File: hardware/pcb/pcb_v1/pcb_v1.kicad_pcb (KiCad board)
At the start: 2 copper layers, 181.4 x 151.5 mm, 21 parts, among them J1 Conn_01x10, J2 Conn_01x10, J3 Conn_01x10, J4 Conn_01x10, U1 Pico

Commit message: pcbv1 updated (MC34166 added)
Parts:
- added D17: 1N5822, Diode_THT:D_DO-201AD_P15.24mm_Horizontal, F.Cu at (184.4, 83.5)
- added U2: MC34166, Package_TO_SOT_SMD:TO-263-5_TabPin3, F.Cu at (175.4, 58.9)

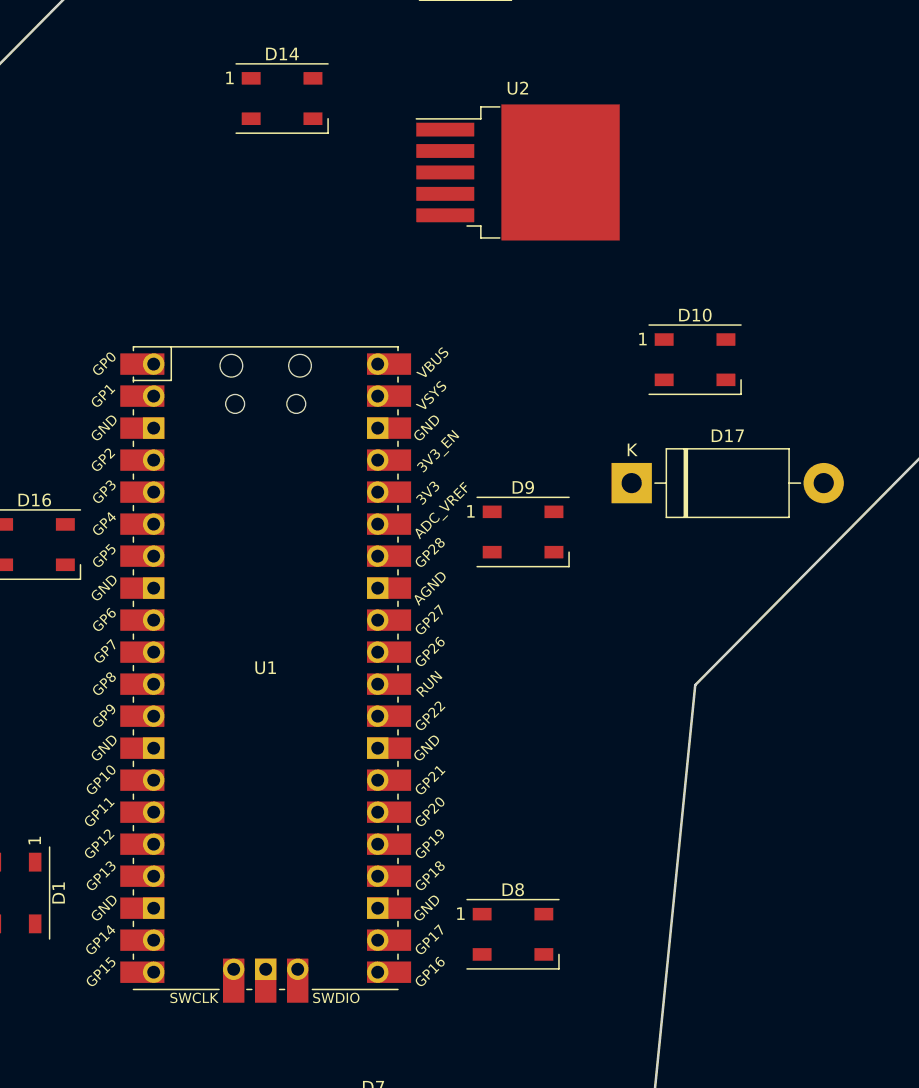
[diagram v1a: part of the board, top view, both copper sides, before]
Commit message: TL2575-05 added
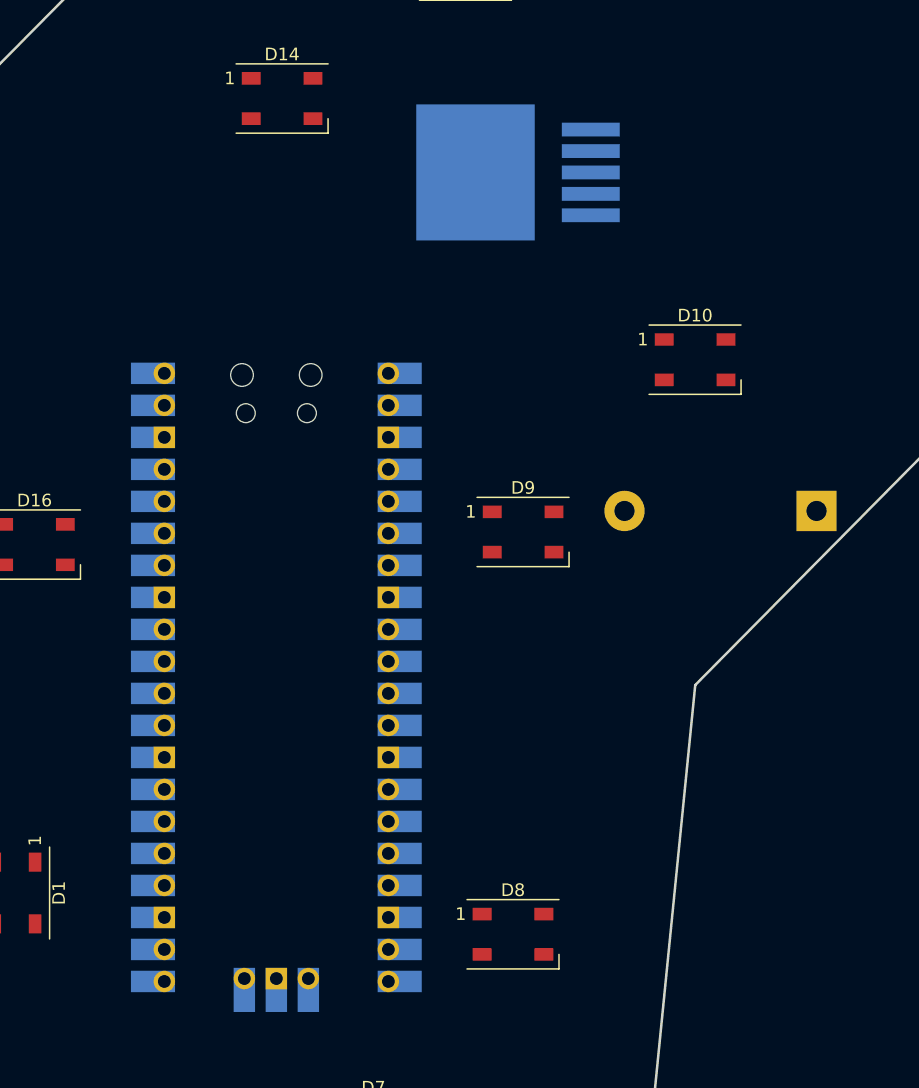
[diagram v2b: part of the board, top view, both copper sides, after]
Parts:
- D17, U1, U2: moved to B.Cu
- moved D17 14.8 mm to (199.1, 85.7), turned to 180 degrees
- moved U1 1.12 mm to (156.2, 98.9), turned to 180 degrees
- turned U2 to 180 degrees

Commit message: worked on pcbv1
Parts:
- added C1: 100nF, Capacitor_SMD:C_0805_2012Metric, F.Cu at (133.7, 111.9)
- added C10: 100nF, Capacitor_SMD:C_0805_2012Metric, F.Cu at (191.2, 77.9)
- added C11: 100nF, Capacitor_SMD:C_0805_2012Metric, F.Cu at (223.5, 51.0)
- added C12: 100nF, Capacitor_SMD:C_0805_2012Metric, F.Cu at (202.3, 37.5)
- added C13: 100nF, Capacitor_SMD:C_0805_2012Metric, F.Cu at (169.5, 38.2)
- added C14: 100nF, Capacitor_SMD:C_0805_2012Metric, F.Cu at (154.9, 48.8)
- added C15: 100nF, Capacitor_SMD:C_0805_2012Metric, F.Cu at (119.4, 76.1)
- added C16: 100nF, Capacitor_SMD:C_0805_2012Metric, F.Cu at (132.7, 90.1)
- added C17: 100uF, Capacitor_SMD:CP_Elec_8x10, B.Cu at (173.0, 91.3)
- added C18: 330uF, Capacitor_SMD:CP_Elec_10x10, B.Cu at (174.7, 130.8)
- added C2: 100nF, Capacitor_SMD:C_0805_2012Metric, F.Cu at (110.9, 120.9)
- added C3: 100nF, Capacitor_SMD:C_0805_2012Metric, F.Cu at (86.8, 141.0)
- added C4: 100nF, Capacitor_SMD:C_0805_2012Metric, F.Cu at (72.6, 164.9)
- added C5: 100nF, Capacitor_SMD:C_0805_2012Metric, F.Cu at (120.4, 165.9)
- added C6: 100nF, Capacitor_SMD:C_0805_2012Metric, F.Cu at (138.9, 161.0)
- added C7: 100nF, Capacitor_SMD:C_0805_2012Metric, F.Cu at (165.7, 139.3)
- added C8: 100nF, Capacitor_SMD:C_0805_2012Metric, F.Cu at (179.3, 117.6)
- added C9: 100nF, Capacitor_SMD:C_0805_2012Metric, F.Cu at (180.2, 85.7)
- added L1: 330uH, Inductor_SMD:L_12x12mm_H8mm, B.Cu at (174.7, 116.5)
- D17: value 1N5822 -> 1N5819; footprint Diode_THT:D_DO-201AD_P15.24mm_Horizontal -> Diode_THT:D_DO-41_SOD81_P10.16mm_Horizontal
- U2: value MC34166 -> TL2575-05
- moved U2 44.4 mm to (176.5, 103.3)
- moved D17 18.5 mm to (183.2, 95.2), turned to 90 degrees
- moved U1 6.43 mm to (150.6, 102.1), turned to 0 degrees
- moved J1 1.64 mm to (234.8, 76.3)
- turned D1 to 0 degrees
- turned D10 to 180 degrees
- turned D11 to -90 degrees
- turned D15 to 90 degrees
- turned D16 to 90 degrees
- turned D2 to 0 degrees
- turned D3 to 0 degrees
- turned D4 to 90 degrees
- turned D5 to 180 degrees
- turned D6 to 180 degrees
- turned D7 to 180 degrees
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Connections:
- D1 pad 4: Net-(D1-Pad4) -> /RGB_IN
- D16 pad 2: Net-(D16-Pad2) -> unconnected-(D16-Pad2)
- D17 pad 1: unconnected-(D17-Pad1) -> Net-(D17-Pad1)
- D17 pad 2: unconnected-(D17-Pad2) -> GND
- J2 pad 10: unconnected-(J2-Pad10) -> +24V
- J2 pad 2: unconnected-(J2-Pad2) -> +24V
- J2 pad 4: unconnected-(J2-Pad4) -> GND
- J2 pad 8: unconnected-(J2-Pad8) -> GND
- J3 pad 10: unconnected-(J3-Pad10) -> +24V
- J3 pad 2: unconnected-(J3-Pad2) -> +24V
- J3 pad 4: unconnected-(J3-Pad4) -> GND
- J3 pad 8: unconnected-(J3-Pad8) -> GND
- J4 pad 10: unconnected-(J4-Pad10) -> +24V
- J4 pad 2: unconnected-(J4-Pad2) -> +24V
- J4 pad 4: unconnected-(J4-Pad4) -> GND
- J4 pad 8: unconnected-(J4-Pad8) -> GND
- U1 pad 13: unconnected-(U1-Pad13) -> GND
- U1 pad 18: unconnected-(U1-Pad18) -> GND
- U1 pad 23: unconnected-(U1-Pad23) -> GND
- U1 pad 26: Net-(D16-Pad2) -> unconnected-(U1-Pad26)
- U1 pad 27: Net-(D1-Pad4) -> unconnected-(U1-Pad27)
- U1 pad 28: unconnected-(U1-Pad28) -> GND
- U1 pad 3: unconnected-(U1-Pad3) -> GND
- U1 pad 33: unconnected-(U1-Pad33) -> GND
- U1 pad 38: unconnected-(U1-Pad38) -> GND
- U1 pad 39: unconnected-(U1-Pad39) -> +5V
- U1 pad 6: unconnected-(U1-Pad6) -> /RGB_IN
- U1 pad 8: unconnected-(U1-Pad8) -> GND
- U2 pad 1: unconnected-(U2-Pad1) -> +24V
- U2 pad 2: unconnected-(U2-Pad2) -> Net-(D17-Pad1)
- U2 pad 3: unconnected-(U2-Pad3) -> GND
- U2 pad 4: unconnected-(U2-Pad4) -> +5V
- U2 pad 5: unconnected-(U2-Pad5) -> GND
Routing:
- net +5V: track 0.00 -> 540.5 mm
- net Net-(D14-Pad2): track 0.00 -> 39.3 mm
- net Net-(D4-Pad2): track 0.00 -> 38.7 mm
- net Net-(D10-Pad2): track 0.00 -> 35.9 mm
- net Net-(D6-Pad2): track 0.00 -> 29.6 mm
- net Net-(D12-Pad2): track 0.00 -> 29.0 mm
- net Net-(D8-Pad2): track 0.00 -> 28.7 mm
- net Net-(D2-Pad2): track 0.00 -> 26.2 mm
- net Net-(D17-Pad1): track 0.00 -> 25.5 mm
- net Net-(D1-Pad2): track 0.00 -> 20.3 mm
- net Net-(D3-Pad2): track 0.00 -> 18.4 mm
- net Net-(D10-Pad4): track 0.00 -> 16.8 mm
- net Net-(D7-Pad2): track 0.00 -> 15.9 mm
- net Net-(D11-Pad2): track 0.00 -> 15.3 mm
- net Net-(D15-Pad2): track 0.00 -> 14.6 mm
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- added copper zone on B.Cu, net GND
- added copper zone on F.Cu, net GND

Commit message: finished pcbv1
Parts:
- added J5: Conn_01x10, Connector_PinHeader_2.54mm:PinHeader_2x05_P2.54mm_Vertical, B.Cu at (210.6, 35.7)
- added J6: Conn_01x10, Connector_PinHeader_2.54mm:PinHeader_2x05_P2.54mm_Vertical, B.Cu at (148.6, 43.0)
- J1, J2, J3, J4: moved to B.Cu
- moved J2 169.6 mm to (110.9, 172.0), turned to -97.2 degrees
- moved J1 123.8 mm to (116.3, 111.9), turned to 121.8 degrees
- moved J3 101.9 mm to (169.3, 145.8), turned to -44.7 degrees
- moved J4 38.0 mm to (222.4, 63.0), turned to -58.2 degrees
- moved C12 7.40 mm to (208.9, 40.8), turned to 90 degrees
- moved C18 0.98 mm to (174.6, 129.8)
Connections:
- J1 pad 1: unconnected-(J1-Pad1) -> /SDA
- J1 pad 10: +24V -> /SCL
- J1 pad 2: +24V -> /SCL
- J1 pad 3: unconnected-(J1-Pad3) -> +24V
- J1 pad 5: unconnected-(J1-Pad5) -> /SEL1
- J1 pad 6: unconnected-(J1-Pad6) -> /SEL1
- J1 pad 7: unconnected-(J1-Pad7) -> +24V
- J1 pad 9: unconnected-(J1-Pad9) -> /SDA
- J2 pad 1: unconnected-(J2-Pad1) -> /SDA
- J2 pad 10: +24V -> /SCL
- J2 pad 2: +24V -> /SCL
- J2 pad 3: unconnected-(J2-Pad3) -> +24V
- J2 pad 5: unconnected-(J2-Pad5) -> /SEL2
- J2 pad 6: unconnected-(J2-Pad6) -> /SEL2
- J2 pad 7: unconnected-(J2-Pad7) -> +24V
- J2 pad 9: unconnected-(J2-Pad9) -> /SDA
- J3 pad 1: unconnected-(J3-Pad1) -> /SDA
- J3 pad 10: +24V -> /SCL
- J3 pad 2: +24V -> /SCL
- J3 pad 3: unconnected-(J3-Pad3) -> +24V
- J3 pad 5: unconnected-(J3-Pad5) -> /SEL3
- J3 pad 6: unconnected-(J3-Pad6) -> /SEL3
- J3 pad 7: unconnected-(J3-Pad7) -> +24V
- J3 pad 9: unconnected-(J3-Pad9) -> /SDA
- J4 pad 1: unconnected-(J4-Pad1) -> /SDA
- J4 pad 10: +24V -> /SCL
- J4 pad 2: +24V -> /SCL
- J4 pad 3: unconnected-(J4-Pad3) -> +24V
- J4 pad 5: unconnected-(J4-Pad5) -> /SEL4
- J4 pad 6: unconnected-(J4-Pad6) -> /SEL4
- J4 pad 7: unconnected-(J4-Pad7) -> +24V
- J4 pad 9: unconnected-(J4-Pad9) -> /SDA
- U1 pad 1: unconnected-(U1-Pad1) -> /SEL3
- U1 pad 2: unconnected-(U1-Pad2) -> /SEL2
- U1 pad 20: unconnected-(U1-Pad20) -> /SEL6
- U1 pad 21: unconnected-(U1-Pad21) -> /SEL5
- U1 pad 22: unconnected-(U1-Pad22) -> /SEL4
- U1 pad 31: unconnected-(U1-Pad31) -> /SDA
- U1 pad 32: unconnected-(U1-Pad32) -> /SCL
- U1 pad 4: unconnected-(U1-Pad4) -> /SEL1
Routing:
- net /SCL: track 0.00 -> 475.2 mm
- net /SDA: track 0.00 -> 403.3 mm
- net +24V: track 11.5 -> 414.8 mm
- net /SEL4: track 0.00 -> 80.2 mm
- net /SEL5: track 0.00 -> 66.4 mm
- net /SEL2: track 0.00 -> 63.6 mm
- net /SEL3: track 0.00 -> 40.3 mm
- net /SEL6: track 0.00 -> 35.2 mm
- net /SEL1: track 0.00 -> 34.1 mm
- net +5V: track 540.5 -> 537.3 mm
- net Net-(D11-Pad2): track 15.3 -> 16.2 mm
